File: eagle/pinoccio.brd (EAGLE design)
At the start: 25.4 x 50.8 mm, 60 parts, among them IC1 ATMEGA16U2QFN32, J1 AVR_SPI_PRG_6, Q1 16MHz, Q2 32.768k, Q3 16MHz, U1 MCP73831, U2 TPS78233, U4 ATMEGA128RFA1, X1 USB-MICROB, Y2 ANTENNA2SMD5

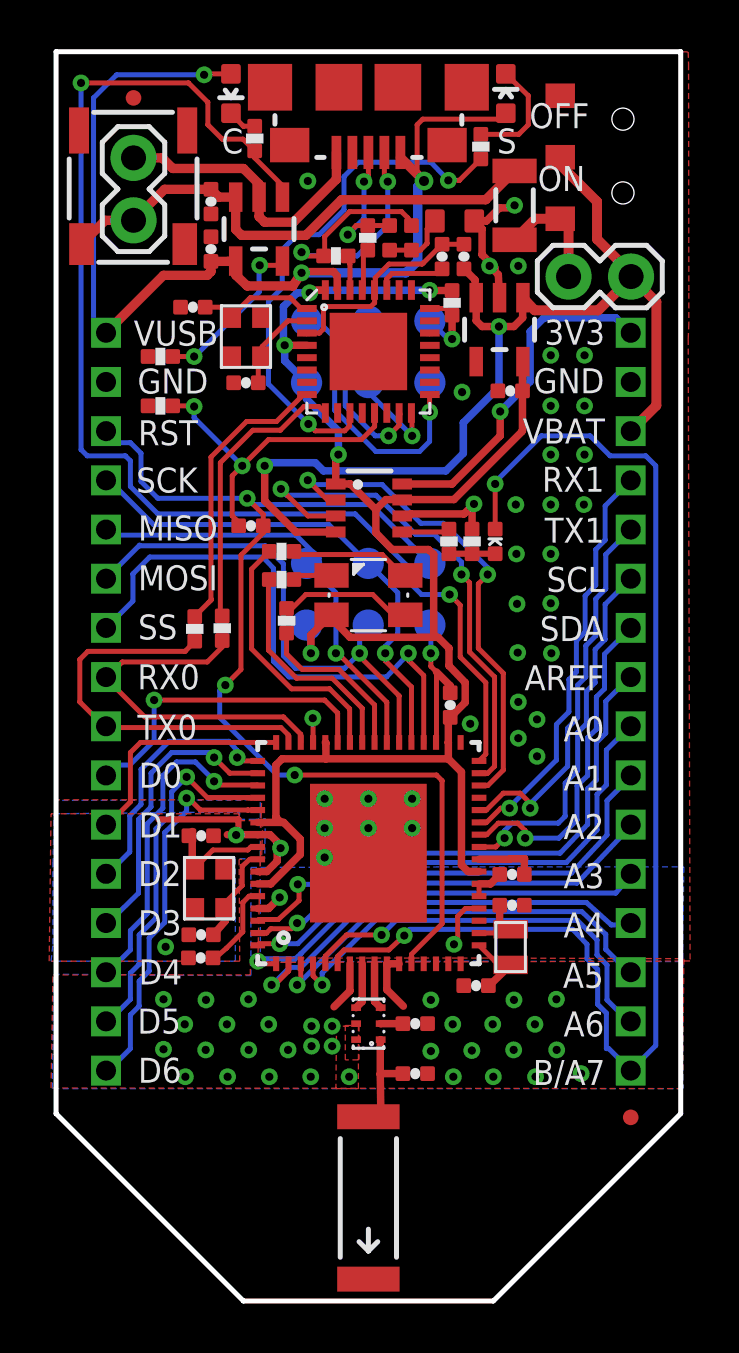
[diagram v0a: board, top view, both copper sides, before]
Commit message: re-cleaned up reset line to 16U2
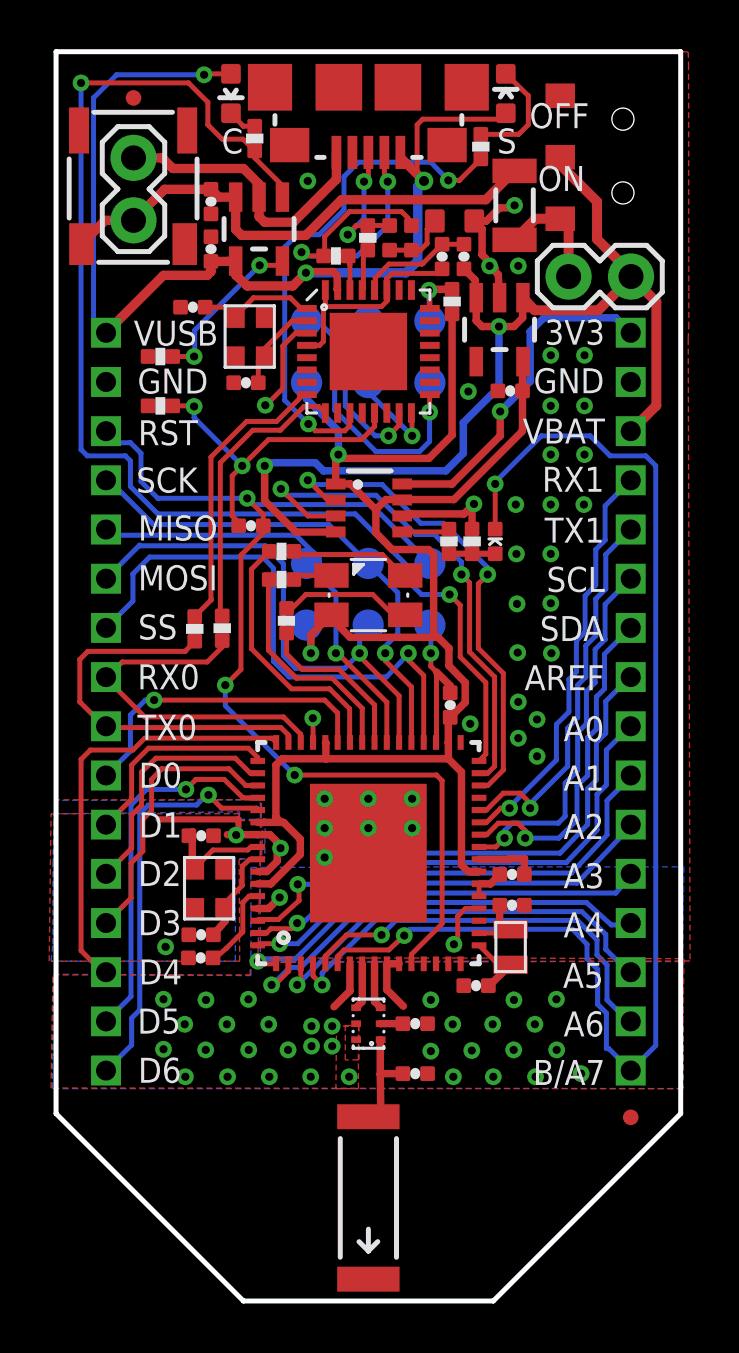
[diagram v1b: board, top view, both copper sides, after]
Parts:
- moved Q3 0.15 mm to (7.87, 39.2)
- moved R1 0.05 mm to (16.1, 40.6), turned to 90 degrees
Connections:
- net D1: now also U4.49; no longer U4.48
- net D2: now also U4.50; no longer U4.49
- net D3: now also U4.51; no longer U4.50
- net D4: now also U4.48; no longer U4.51
- net N$12: now also IC1.32, IC1.4
- net VCC: no longer IC1.32, IC1.4
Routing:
- net N$12: track 2.93 -> 9.02 mm
- net D4: track 13.5 -> 17.5 mm, vias 1 -> 0
- net VCC: track 71.5 -> 69.3 mm, vias 5 -> 2
- net D1: track 9.50 -> 8.56 mm
- net D6: track 15.6 -> 16.4 mm
- net D2: track 10.6 -> 9.94 mm, vias 1 -> 0
- net RESET: track 45.4 -> 44.8 mm
- net D3: track 12.0 -> 11.4 mm, vias 1 -> 0
- net N$59: track 21.4 -> 20.9 mm
- net GND: track 55.8 -> 55.5 mm, vias 73 -> 74

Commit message: Added new socker header datasheet
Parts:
- C2: value 4.7uF -> 1.0uF
- R14, R3: value 1k -> 470
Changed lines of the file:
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@@
 </autorouter>
 <elements>
-<element name="C2" library="Pinoccio" package="0402-CAP" value="4.7uF" x="18.4658" y="37.0078" smashed="yes" rot="R180"/>
+<element name="C2" library="Pinoccio" package="0402-CAP" value="1.0uF" x="18.4658" y="37.0078" smashed="yes" rot="R180"/>
 <element name="JP4" library="Pinoccio" package="2X3-PAD" value="AVR_SPI" x="10.1854" y="29.99231875" smashed="yes" rot="MR180"/>
 <element name="U2" library="SparkFun" package="SOT23-5" value="TPS78233" x="18.034" y="39.497" smashed="yes" rot="R180"/>
@@
 <element name="C5" library="Pinoccio" package="0402-CAP" value="4.7uF" x="6.2992" y="44.704" smashed="yes" rot="R270"/>
 <element name="D2" library="Pinoccio" package="LED-0603" value="Yellow" x="7.112" y="49.0982" smashed="yes" rot="R180"/>
-<element name="R3" library="Pinoccio" package="0402-RES" value="1k" x="8.0772" y="47.2694" smashed="yes" rot="R90"/>
+<element name="R3" library="Pinoccio" package="0402-RES" value="470" x="8.0772" y="47.2694" smashed="yes" rot="R90"/>
 <element name="X1" library="Pinoccio" package="USB-MICROB" value="USB-MICROB" x="12.7" y="49.3522" locked="yes" smashed="yes" rot="R180"/>
 <element name="F1" library="SparkFun" package="PTC-1206" value="PTCSMD" x="18.6436" y="44.5516" smashed="yes" rot="R270"/>
@@
 <element name="J1" library="Pinoccio" package="2X3-PAD" value="AVR_SPI_PRG_6" x="10.1854" y="39.8526" rot="MR180"/>
 <element name="D1" library="Pinoccio" package="LED-0603" value="Green" x="18.288" y="49.0982" smashed="yes"/>
-<element name="R14" library="Pinoccio" package="0402-RES" value="1k" x="17.272" y="46.9392" smashed="yes" rot="R90"/>
+<element name="R14" library="Pinoccio" package="0402-RES" value="470" x="17.272" y="46.9392" smashed="yes" rot="R90"/>
 <element name="R18" library="Pinoccio" package="0402-RES" value="470" x="9.3726" y="27.6606" smashed="yes" rot="R90"/>
 <element name="JP3" library="Pinoccio" package="MICRO-FIDUCIAL" value="FIDUCIALUFIDUCIAL" x="23.368" y="7.4676"/>
@@
 </signal>
 </signals>
-<errors>
-</errors>
 </board>
 </drawing>

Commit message: Moar fixups
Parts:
- C2: value 1.0uF -> 2.2uF
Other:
- board text added: "128RFA1"
- board text removed: "128RFR2"
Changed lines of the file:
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@@
 <text x="17.9324" y="46.6598" size="1.016" layer="21" font="vector" ratio="15">S</text>
 <text x="14.1478" y="41.5036" size="0.8128" layer="22" font="vector" ratio="15" rot="MR0">16U2</text>
-<text x="15.0876" y="31.7754" size="0.8128" layer="22" font="vector" ratio="15" rot="MR0">128RFR2</text>
+<text x="15.0876" y="31.7754" size="0.8128" layer="22" font="vector" ratio="15" rot="MR0">128RFA1</text>
 </plain>
 <attributes>
@@
 </autorouter>
 <elements>
-<element name="C2" library="Pinoccio" package="0402-CAP" value="1.0uF" x="18.4658" y="37.0078" smashed="yes" rot="R180"/>
+<element name="C2" library="Pinoccio" package="0402-CAP" value="2.2uF" x="18.4658" y="37.0078" smashed="yes" rot="R180"/>
 <element name="JP4" library="Pinoccio" package="2X3-PAD" value="AVR_SPI" x="10.1854" y="29.99231875" smashed="yes" rot="MR180"/>
 <element name="U2" library="SparkFun" package="SOT23-5" value="TPS78233" x="18.034" y="39.497" smashed="yes" rot="R180"/>
@@
 <wire x1="18.9404" y1="35.3488" x2="18.9658" y2="35.3996" width="0.3048" layer="1"/>
 <wire x1="18.9658" y1="35.3996" x2="18.9658" y2="37.0078" width="0.3048" layer="1"/>
-<wire x1="18.984" y1="38.1969" x2="18.9658" y2="38.1787" width="0.3048" layer="1"/>
-<wire x1="18.9658" y1="38.1787" x2="18.9658" y2="37.0078" width="0.3048" layer="1"/>
 <contactref element="R1" pad="1"/>
 <contactref element="J1" pad="2"/>
@@
 <wire x1="15.1638" y1="34.2646" x2="11.6332" y2="34.2646" width="0.3048" layer="1"/>
 <wire x1="11.6332" y1="34.2646" x2="11.4808" y2="34.417" width="0.3048" layer="1"/>
+<wire x1="18.984" y1="38.1969" x2="18.9658" y2="38.1787" width="0.3048" layer="1"/>
+<wire x1="18.9658" y1="38.1787" x2="18.9658" y2="37.0078" width="0.3048" layer="1"/>
 </signal>
 <signal name="MOSI">
@@
 <wire x1="18.6182" y1="39.624" x2="18.9738" y2="39.9796" width="0.3048" layer="1"/>
 <wire x1="18.9738" y1="39.9796" x2="18.9738" y2="40.4059" width="0.3048" layer="1"/>
-<wire x1="18.9738" y1="40.4059" x2="18.984" y2="40.7971" width="0.3048" layer="1"/>
-<wire x1="22.0472" y1="40.2844" x2="19.4619" y2="40.2844" width="0.4064" layer="1"/>
 <wire x1="19.4619" y1="40.2844" x2="18.984" y2="40.7971" width="0.4064" layer="1"/>
 <wire x1="17.084" y1="40.7971" x2="17.0332" y2="41.5218" width="0.3048" layer="1"/>
@@
 <wire x1="11.3684" y1="31.2674" x2="11.3728" y2="31.2718" width="0.3048" layer="1"/>
 <wire x1="16.5608" y1="34.4678" x2="16.5608" y2="35.7124" width="0.3048" layer="16"/>
+<wire x1="18.0086" y1="37.1602" x2="18.0086" y2="39.624" width="0.3048" layer="16"/>
 <wire x1="16.5608" y1="35.7124" x2="18.0086" y2="37.1602" width="0.3048" layer="16"/>
-<wire x1="18.0086" y1="37.1602" x2="18.0086" y2="39.624" width="0.3048" layer="16"/>
+<wire x1="18.9738" y1="40.4059" x2="18.984" y2="40.7971" width="0.3048" layer="1"/>
+<wire x1="22.0472" y1="40.2844" x2="19.4619" y2="40.2844" width="0.4064" layer="1"/>
 </signal>
 <signal name="N$11">
@@
 <wire x1="3.4544" y1="33.3248" x2="4.1402" y2="32.639" width="0.2032" layer="16"/>
 <wire x1="4.1402" y1="32.639" x2="7.7724" y2="32.639" width="0.2032" layer="16"/>
+<wire x1="6.8834" y1="24.2062" x2="6.8834" y2="25.0444" width="0.2032" layer="16"/>
 <wire x1="9.7028" y1="21.3868" x2="6.8834" y2="24.2062" width="0.2032" layer="16"/>
-<wire x1="6.8834" y1="24.2062" x2="6.8834" y2="25.0444" width="0.2032" layer="16"/>
 </signal>
 <signal name="N$20">

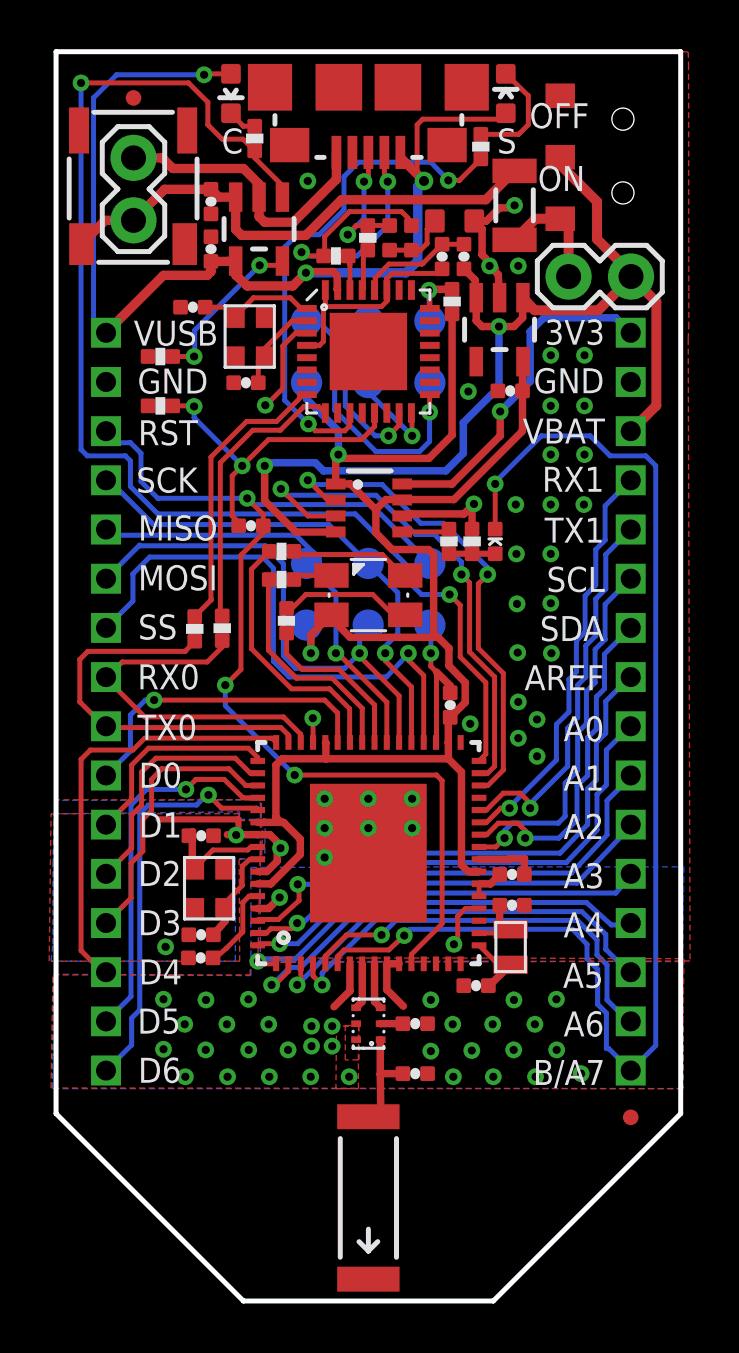
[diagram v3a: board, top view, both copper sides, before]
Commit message: Fix up library naming
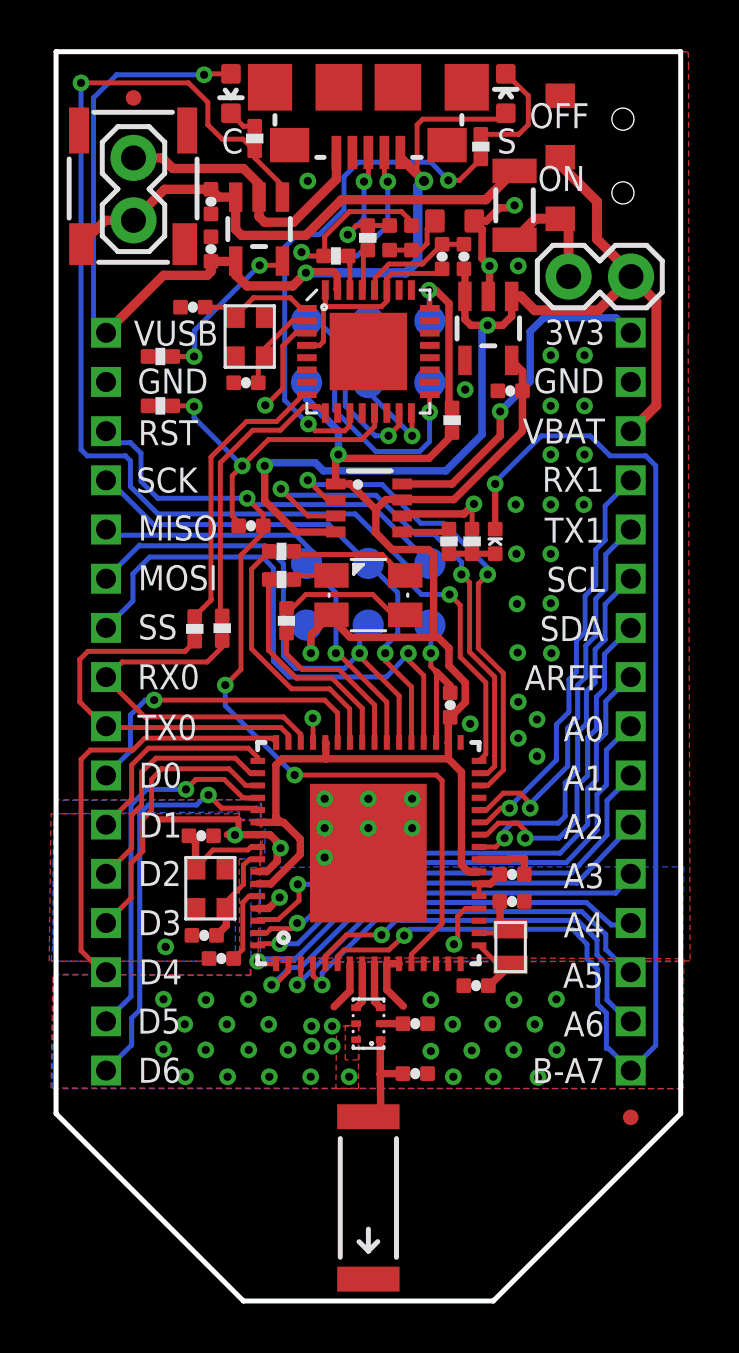
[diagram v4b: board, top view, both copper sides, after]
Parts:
- D3: value DIODE-SCHOTTKY -> DIODE-SCHOTTKY0402
- U2: device SparkFun:SOT23-5 -> Pinoccio:SOT23-5
- moved R1 4.83 mm to (16.1, 35.8)
- moved C7 0.84 mm to (6.72, 13.9)
- moved U2 0.46 mm to (17.6, 39.5)
- moved C15 0.15 mm to (18.5, 16.2)
- moved C12 0.13 mm to (6.02, 14.9)
- moved Q1 0.05 mm to (6.27, 16.8)
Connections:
- net USB_VIN renamed VUSB
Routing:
- net VCC: track 69.3 -> 64.6 mm
- net N$7: track 2.96 -> 7.34 mm
- net GND: track 55.5 -> 55.2 mm, vias 74 -> 73
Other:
- board text added: "B-A7"
- board text removed: "B/A7"

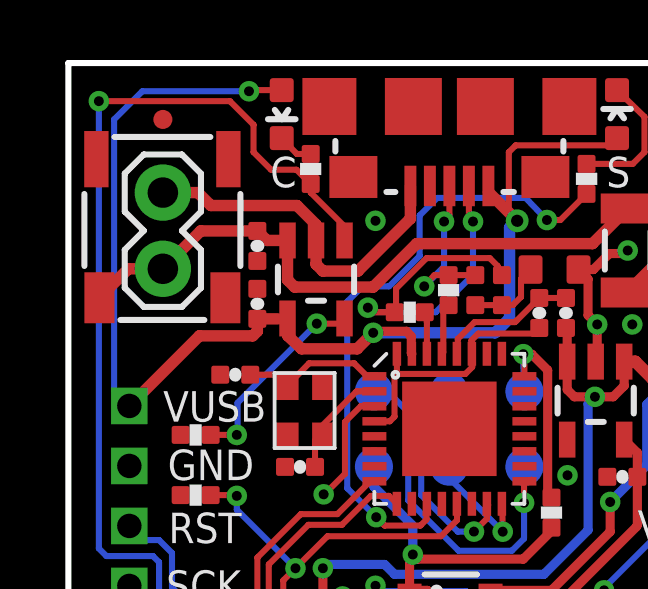
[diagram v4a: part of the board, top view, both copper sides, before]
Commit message: move charge LED anode side to vbat instead of vusb
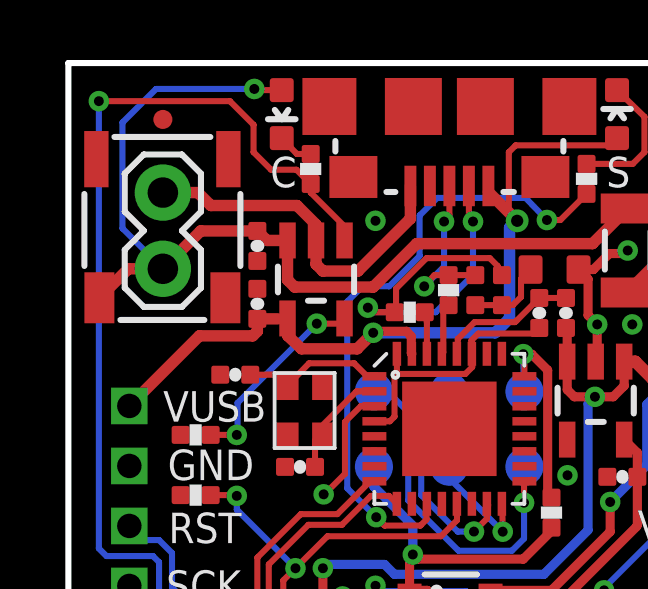
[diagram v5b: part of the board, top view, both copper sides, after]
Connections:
- net VBAT: now also D2.A
- net VUSB: no longer D2.A
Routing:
- net VUSB: track 44.2 -> 28.4 mm, vias 3 -> 2
- net VBAT: track 21.2 -> 32.4 mm, vias 0 -> 1
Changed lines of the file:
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@@
 <contactref element="X1" pad="VBUS"/>
 <contactref element="C4" pad="1"/>
-<contactref element="D2" pad="A"/>
 <contactref element="JP-L" pad="P$1"/>
 <contactref element="IC1" pad="31"/>
@@
 <wire x1="6.1468" y1="41.7068" x2="4.3688" y2="41.7068" width="0.381" layer="1"/>
 <wire x1="4.3688" y1="41.7068" x2="2.032" y2="39.37" width="0.381" layer="1"/>
-<wire x1="7.112" y1="49.8982" x2="6.0578" y2="49.8982" width="0.2032" layer="1"/>
-<wire x1="6.0578" y1="49.8982" x2="6.0198" y2="49.8602" width="0.2032" layer="1"/>
-<via x="6.0198" y="49.8602" extent="1-16" drill="0.3302"/>
-<wire x1="6.0198" y1="49.8602" x2="2.4638" y2="49.8602" width="0.2032" layer="16"/>
-<wire x1="2.4638" y1="49.8602" x2="1.524" y2="48.9204" width="0.2032" layer="16"/>
-<wire x1="1.524" y1="48.9204" x2="1.524" y2="39.878" width="0.2032" layer="16"/>
-<wire x1="1.524" y1="39.878" x2="2.032" y2="39.37" width="0.2032" layer="16"/>
 <wire x1="14.9606" y1="45.5422" x2="14.6812" y2="45.8216" width="0.2032" layer="1"/>
 <wire x1="14.6812" y1="45.8216" x2="14.6812" y2="47.8282" width="0.2032" layer="1"/>
@@
 <wire x1="10.16" y1="43.3324" x2="11.6078" y2="44.7802" width="0.381" layer="1"/>
 <wire x1="11.6078" y1="44.7802" x2="17.4722" y2="44.7802" width="0.381" layer="1"/>
+<contactref element="D2" pad="A"/>
+<wire x1="7.112" y1="49.8982" x2="6.2358" y2="49.8982" width="0.2032" layer="1"/>
+<wire x1="6.2358" y1="49.8982" x2="6.1976" y2="49.9364" width="0.2032" layer="1"/>
+<via x="6.1976" y="49.9364" extent="1-16" drill="0.3302"/>
+<wire x1="6.1976" y1="49.9364" x2="2.921" y2="49.9364" width="0.2032" layer="16"/>
+<wire x1="2.921" y1="49.9364" x2="1.8034" y2="48.8188" width="0.2032" layer="16"/>
+<wire x1="1.8034" y1="48.8188" x2="1.8034" y2="45.2882" width="0.2032" layer="16"/>
+<wire x1="1.8034" y1="45.2882" x2="3.1496" y2="43.942" width="0.2032" layer="16"/>
 </signal>
 <signal name="VBAT-AE">
